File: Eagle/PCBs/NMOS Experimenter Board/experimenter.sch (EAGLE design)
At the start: 0 parts

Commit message: Update packages
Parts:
- added D10, D11, D12, D13, D14, D15, D16, D17, D18, D19, D2, D20, D21, D22, D23, D24, D25, D3, D4, D5, D6, D7, D8, D9: (no value), ellajameson-core:LED0603
- added DRAINA10, DRAINA11, DRAINA12, DRAINA13, DRAINA14, DRAINA15, DRAINA16, DRAINA17, DRAINA18, DRAINA19, DRAINA2, DRAINA20, DRAINA21, DRAINA22, DRAINA23, DRAINA24, DRAINA25, DRAINA3, DRAINA4, DRAINA5, DRAINA6, DRAINA7, DRAINA8, DRAINA9, DRAINB10, DRAINB11, DRAINB12, DRAINB13, DRAINB14, DRAINB15, DRAINB16, DRAINB17, DRAINB18, DRAINB19, DRAINB2, DRAINB20, DRAINB21, DRAINB22, DRAINB23, DRAINB24, DRAINB25, DRAINB3, DRAINB4, DRAINB5, DRAINB6, DRAINB7, DRAINB8, DRAINB9, DRAINC10, DRAINC11, DRAINC12, DRAINC13, DRAINC14, DRAINC15, DRAINC16, DRAINC17, DRAINC18, DRAINC19, DRAINC2, DRAINC20, DRAINC21, DRAINC22, DRAINC23, DRAINC24, DRAINC25, DRAINC3, DRAINC4, DRAINC5, DRAINC6, DRAINC7, DRAINC8, DRAINC9, DRAIND10, DRAIND11, DRAIND12, DRAIND13, DRAIND14, DRAIND15, DRAIND16, DRAIND17, DRAIND18, DRAIND19, DRAIND2, DRAIND20, DRAIND21, DRAIND22, DRAIND23, DRAIND24, DRAIND25, DRAIND3, DRAIND4, DRAIND5, DRAIND6, DRAIND7, DRAIND8, DRAIND9, GATE10, GATE11, GATE12, GATE13, GATE14, GATE15, GATE16, GATE17, GATE18, GATE19, GATE2, GATE20, GATE21, GATE22, GATE23, GATE24, GATE25, GATE3, GATE4, GATE5, GATE6, GATE7, GATE8, GATE9, SOURCEA10, SOURCEA11, SOURCEA12, SOURCEA13, SOURCEA14, SOURCEA15, SOURCEA16, SOURCEA17, SOURCEA18, SOURCEA19, SOURCEA2, SOURCEA20, SOURCEA21, SOURCEA22, SOURCEA23, SOURCEA24, SOURCEA25, SOURCEA3, SOURCEA4, SOURCEA5, SOURCEA6, SOURCEA7, SOURCEA8, SOURCEA9, SOURCEB10, SOURCEB11, SOURCEB12, SOURCEB13, SOURCEB14, SOURCEB15, SOURCEB16, SOURCEB17, SOURCEB18, SOURCEB19, SOURCEB2, SOURCEB20, SOURCEB21, SOURCEB22, SOURCEB23, SOURCEB24, SOURCEB25, SOURCEB3, SOURCEB4, SOURCEB5, SOURCEB6, SOURCEB7, SOURCEB8, SOURCEB9, SOURCEC10, SOURCEC11, SOURCEC12, SOURCEC13, SOURCEC14, SOURCEC15, SOURCEC16, SOURCEC17, SOURCEC18, SOURCEC19, SOURCEC2, SOURCEC20, SOURCEC21, SOURCEC22, SOURCEC23, SOURCEC24, SOURCEC25, SOURCEC3, SOURCEC4, SOURCEC5, SOURCEC6, SOURCEC7, SOURCEC8, SOURCEC9, SOURCED10, SOURCED11, SOURCED12, SOURCED13, SOURCED14, SOURCED15, SOURCED16, SOURCED17, SOURCED18, SOURCED19, SOURCED2, SOURCED20, SOURCED21, SOURCED22, SOURCED23, SOURCED24, SOURCED25, SOURCED3, SOURCED4, SOURCED5, SOURCED6, SOURCED7, SOURCED8, SOURCED9: TPWIRE, ellajameson-core:TPWIRE
- added JD10, JD11, JD12, JD13, JD14, JD15, JD16, JD17, JD18, JD19, JD2, JD20, JD21, JD22, JD23, JD24, JD25, JD3, JD4, JD5, JD6, JD7, JD8, JD9, JN10, JN11, JN12, JN13, JN14, JN15, JN16, JN17, JN18, JN19, JN2, JN20, JN21, JN22, JN23, JN24, JN25, JN3, JN4, JN5, JN6, JN7, JN8, JN9, JP10, JP11, JP12, JP13, JP14, JP15, JP16, JP17, JP18, JP19, JP2, JP20, JP21, JP22, JP23, JP24, JP25, JP3, JP4, JP5, JP6, JP7, JP8, JP9, JS10, JS11, JS12, JS13, JS14, JS15, JS16, JS17, JS18, JS19, JS2, JS20, JS21, JS22, JS23, JS24, JS25, JS3, JS4, JS5, JS6, JS7, JS8, JS9: SJ_NO, ellajameson-core:SJ_NO
- added Q10, Q11, Q12, Q13, Q14, Q15, Q16, Q17, Q18, Q19, Q2, Q20, Q21, Q22, Q23, Q24, Q25, Q3, Q4, Q5, Q6, Q7, Q8, Q9: 2N7002, ellajameson-core:2N7002
- added R10, R11, R12, R13, R14, R15, R16, R17, R18, R19, R2, R20, R21, R22, R23, R24, R25, R3, R4, R5, R6, R7, R8, R9: (no value), ellajameson-core:RES0603
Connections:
- new net GND: JN10.1, JN11.1, JN12.1, JN13.1, JN14.1, JN15.1, JN16.1, JN17.1, JN18.1, JN19.1, JN2.1, JN20.1, JN21.1, JN22.1, JN23.1, JN24.1, JN25.1, JN3.1, JN4.1, JN5.1, JN6.1, JN7.1, JN8.1, JN9.1
- new net N$1: D2.A, JP2.2, R2.1
- new net N$10: D3.K, DRAINA3.S, DRAINB3.S, DRAINC3.S, DRAIND3.S, JD3.2, JD4.1, JP3.1, JS12.1, Q3.D
- new net N$100: GATE25.S, Q25.G
- new net N$11: JN3.2, JS3.2, Q3.S, SOURCEA3.S, SOURCEB3.S, SOURCEC3.S, SOURCED3.S
- new net N$12: GATE3.S, Q3.G
- new net N$13: D4.A, JP4.2, R4.1
- new net N$14: D4.K, DRAINA4.S, DRAINB4.S, DRAINC4.S, DRAIND4.S, JD2.1, JD4.2, JP4.1, JS11.1, Q4.D
- new net N$15: JN4.2, JS4.2, Q4.S, SOURCEA4.S, SOURCEB4.S, SOURCEC4.S, SOURCED4.S
- new net N$16: GATE4.S, Q4.G
- new net N$17: D5.A, JP5.2, R5.1
- new net N$18: D5.K, DRAINA5.S, DRAINB5.S, DRAINC5.S, DRAIND5.S, JD3.1, JD5.2, JP5.1, JS13.1, Q5.D
- new net N$19: JN5.2, JS5.2, Q5.S, SOURCEA5.S, SOURCEB5.S, SOURCEC5.S, SOURCED5.S
- new net N$2: D2.K, DRAINA2.S, DRAINB2.S, DRAINC2.S, DRAIND2.S, JD2.2, JP2.1, JS10.1, Q2.D
- new net N$20: GATE5.S, Q5.G
- new net N$21: D6.A, JP6.2, R6.1
- new net N$22: D6.K, DRAINA6.S, DRAINB6.S, DRAINC6.S, DRAIND6.S, JD5.1, JD6.2, JP6.1, JS14.1, Q6.D
- new net N$23: JN6.2, JS6.2, Q6.S, SOURCEA6.S, SOURCEB6.S, SOURCEC6.S, SOURCED6.S
- new net N$24: GATE6.S, Q6.G
- new net N$25: D7.A, JP7.2, R7.1
- new net N$26: D7.K, DRAINA7.S, DRAINB7.S, DRAINC7.S, DRAIND7.S, JD6.1, JD7.2, JP7.1, JS15.1, Q7.D
- new net N$27: JN7.2, JS7.2, Q7.S, SOURCEA7.S, SOURCEB7.S, SOURCEC7.S, SOURCED7.S
- new net N$28: GATE7.S, Q7.G
- new net N$29: D8.A, JP8.2, R8.1
- new net N$3: JN2.2, JS2.2, Q2.S, SOURCEA2.S, SOURCEB2.S, SOURCEC2.S, SOURCED2.S
- new net N$30: D8.K, DRAINA8.S, DRAINB8.S, DRAINC8.S, DRAIND8.S, JD7.1, JD8.2, JP8.1, JS16.1, Q8.D
- new net N$31: JN8.2, JS8.2, Q8.S, SOURCEA8.S, SOURCEB8.S, SOURCEC8.S, SOURCED8.S
- new net N$32: GATE8.S, Q8.G
- new net N$33: D9.A, JP9.2, R9.1
- new net N$34: D9.K, DRAINA9.S, DRAINB9.S, DRAINC9.S, DRAIND9.S, JD8.1, JD9.2, JP9.1, JS17.1, Q9.D
- new net N$35: JN9.2, JS9.2, Q9.S, SOURCEA9.S, SOURCEB9.S, SOURCEC9.S, SOURCED9.S
- new net N$36: GATE9.S, Q9.G
- new net N$37: D10.A, JP10.2, R10.1
- new net N$38: D10.K, DRAINA10.S, DRAINB10.S, DRAINC10.S, DRAIND10.S, JD10.2, JP10.1, JS18.1, Q10.D
- new net N$39: JN10.2, JS10.2, Q10.S, SOURCEA10.S, SOURCEB10.S, SOURCEC10.S, SOURCED10.S
- new net N$4: GATE2.S, Q2.G
- new net N$40: GATE10.S, Q10.G
- new net N$41: D11.A, JP11.2, R11.1
- new net N$42: D11.K, DRAINA11.S, DRAINB11.S, DRAINC11.S, DRAIND11.S, JD10.1, JD11.2, JP11.1, JS19.1, Q11.D
- new net N$43: JN11.2, JS11.2, Q11.S, SOURCEA11.S, SOURCEB11.S, SOURCEC11.S, SOURCED11.S
- new net N$44: GATE11.S, Q11.G
- new net N$45: D12.A, JP12.2, R12.1
- new net N$46: D12.K, DRAINA12.S, DRAINB12.S, DRAINC12.S, DRAIND12.S, JD11.1, JD12.2, JP12.1, JS20.1, Q12.D
- new net N$47: JN12.2, JS12.2, Q12.S, SOURCEA12.S, SOURCEB12.S, SOURCEC12.S, SOURCED12.S
- new net N$48: GATE12.S, Q12.G
- new net N$49: D13.A, JP13.2, R13.1
- new net N$50: D13.K, DRAINA13.S, DRAINB13.S, DRAINC13.S, DRAIND13.S, JD12.1, JD13.2, JP13.1, JS21.1, Q13.D
- new net N$51: JN13.2, JS13.2, Q13.S, SOURCEA13.S, SOURCEB13.S, SOURCEC13.S, SOURCED13.S
- new net N$52: GATE13.S, Q13.G
- new net N$53: D14.A, JP14.2, R14.1
- new net N$54: D14.K, DRAINA14.S, DRAINB14.S, DRAINC14.S, DRAIND14.S, JD13.1, JD14.2, JP14.1, JS22.1, Q14.D
- new net N$55: JN14.2, JS14.2, Q14.S, SOURCEA14.S, SOURCEB14.S, SOURCEC14.S, SOURCED14.S
- new net N$56: GATE14.S, Q14.G
- new net N$57: D15.A, JP15.2, R15.1
- new net N$58: D15.K, DRAINA15.S, DRAINB15.S, DRAINC15.S, DRAIND15.S, JD14.1, JD15.2, JP15.1, JS23.1, Q15.D
- new net N$59: JN15.2, JS15.2, Q15.S, SOURCEA15.S, SOURCEB15.S, SOURCEC15.S, SOURCED15.S
- new net N$60: GATE15.S, Q15.G
- new net N$61: D16.A, JP16.2, R16.1
- new net N$62: D16.K, DRAINA16.S, DRAINB16.S, DRAINC16.S, DRAIND16.S, JD15.1, JD16.2, JP16.1, JS24.1, Q16.D
- new net N$63: JN16.2, JS16.2, Q16.S, SOURCEA16.S, SOURCEB16.S, SOURCEC16.S, SOURCED16.S
- new net N$64: GATE16.S, Q16.G
- new net N$65: D17.A, JP17.2, R17.1
- new net N$66: D17.K, DRAINA17.S, DRAINB17.S, DRAINC17.S, DRAIND17.S, JD16.1, JD17.2, JP17.1, JS25.1, Q17.D
- new net N$67: JN17.2, JS17.2, Q17.S, SOURCEA17.S, SOURCEB17.S, SOURCEC17.S, SOURCED17.S
- new net N$68: GATE17.S, Q17.G
- new net N$69: D18.A, JP18.2, R18.1
- new net N$70: D18.K, DRAINA18.S, DRAINB18.S, DRAINC18.S, DRAIND18.S, JD18.2, JP18.1, Q18.D
- new net N$71: JN18.2, JS18.2, Q18.S, SOURCEA18.S, SOURCEB18.S, SOURCEC18.S, SOURCED18.S
- new net N$72: GATE18.S, Q18.G
- new net N$73: D19.A, JP19.2, R19.1
- new net N$74: D19.K, DRAINA19.S, DRAINB19.S, DRAINC19.S, DRAIND19.S, JD18.1, JD19.2, JP19.1, Q19.D
- new net N$75: JN19.2, JS19.2, Q19.S, SOURCEA19.S, SOURCEB19.S, SOURCEC19.S, SOURCED19.S
- new net N$76: GATE19.S, Q19.G
- new net N$77: D20.A, JP20.2, R20.1
- new net N$78: D20.K, DRAINA20.S, DRAINB20.S, DRAINC20.S, DRAIND20.S, JD19.1, JD20.2, JP20.1, Q20.D
- new net N$79: JN20.2, JS20.2, Q20.S, SOURCEA20.S, SOURCEB20.S, SOURCEC20.S, SOURCED20.S
- new net N$80: GATE20.S, Q20.G
- new net N$81: D21.A, JP21.2, R21.1
- new net N$82: D21.K, DRAINA21.S, DRAINB21.S, DRAINC21.S, DRAIND21.S, JD20.1, JD21.2, JP21.1, Q21.D
- new net N$83: JN21.2, JS21.2, Q21.S, SOURCEA21.S, SOURCEB21.S, SOURCEC21.S, SOURCED21.S
- new net N$84: GATE21.S, Q21.G
- new net N$85: D22.A, JP22.2, R22.1
- new net N$86: D22.K, DRAINA22.S, DRAINB22.S, DRAINC22.S, DRAIND22.S, JD21.1, JD22.2, JP22.1, Q22.D
- new net N$87: JN22.2, JS22.2, Q22.S, SOURCEA22.S, SOURCEB22.S, SOURCEC22.S, SOURCED22.S
- new net N$88: GATE22.S, Q22.G
- new net N$89: D23.A, JP23.2, R23.1
- new net N$9: D3.A, JP3.2, R3.1
- new net N$90: D23.K, DRAINA23.S, DRAINB23.S, DRAINC23.S, DRAIND23.S, JD22.1, JD23.2, JP23.1, Q23.D
- new net N$91: JN23.2, JS23.2, Q23.S, SOURCEA23.S, SOURCEB23.S, SOURCEC23.S, SOURCED23.S
- new net N$92: GATE23.S, Q23.G
- new net N$93: D24.A, JP24.2, R24.1
- new net N$94: D24.K, DRAINA24.S, DRAINB24.S, DRAINC24.S, DRAIND24.S, JD23.1, JD24.2, JP24.1, Q24.D
- new net N$95: JN24.2, JS24.2, Q24.S, SOURCEA24.S, SOURCEB24.S, SOURCEC24.S, SOURCED24.S
- new net N$96: GATE24.S, Q24.G
- new net N$97: D25.A, JP25.2, R25.1
- new net N$98: D25.K, DRAINA25.S, DRAINB25.S, DRAINC25.S, DRAIND25.S, JD24.1, JD25.2, JP25.1, Q25.D
- new net N$99: JN25.2, JS25.2, Q25.S, SOURCEA25.S, SOURCEB25.S, SOURCEC25.S, SOURCED25.S
- new net VCC: R10.2, R11.2, R12.2, R13.2, R14.2, R15.2, R16.2, R17.2, R18.2, R19.2, R2.2, R20.2, R21.2, R22.2, R23.2, R24.2, R25.2, R3.2, R4.2, R5.2, R6.2, R7.2, R8.2, R9.2
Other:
- note added: "NMOS Logic Transistor Cell"

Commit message: A 6x12 grid fits
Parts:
- added D26, D27, D28, D29, D30, D31, D32, D33, D34, D35, D36, D37, D38, D39, D40, D41, D42, D43, D44, D45, D46, D47, D48, D49, D50, D51, D52, D53, D54, D55, D56, D57, D58, D59, D60, D61, D62, D63, D64, D65, D66, D67, D68, D69, D70, D71, D72, D73: (no value), ellajameson-core:LED0603
- added DRAINA26, DRAINA27, DRAINA28, DRAINA29, DRAINA30, DRAINA31, DRAINA32, DRAINA33, DRAINA34, DRAINA35, DRAINA36, DRAINA37, DRAINA38, DRAINA39, DRAINA40, DRAINA41, DRAINA42, DRAINA43, DRAINA44, DRAINA45, DRAINA46, DRAINA47, DRAINA48, DRAINA49, DRAINA50, DRAINA51, DRAINA52, DRAINA53, DRAINA54, DRAINA55, DRAINA56, DRAINA57, DRAINA58, DRAINA59, DRAINA60, DRAINA61, DRAINA62, DRAINA63, DRAINA64, DRAINA65, DRAINA66, DRAINA67, DRAINA68, DRAINA69, DRAINA70, DRAINA71, DRAINA72, DRAINA73, DRAINB26, DRAINB27, DRAINB28, DRAINB29, DRAINB30, DRAINB31, DRAINB32, DRAINB33, DRAINB34, DRAINB35, DRAINB36, DRAINB37, DRAINB38, DRAINB39, DRAINB40, DRAINB41, DRAINB42, DRAINB43, DRAINB44, DRAINB45, DRAINB46, DRAINB47, DRAINB48, DRAINB49, DRAINB50, DRAINB51, DRAINB52, DRAINB53, DRAINB54, DRAINB55, DRAINB56, DRAINB57, DRAINB58, DRAINB59, DRAINB60, DRAINB61, DRAINB62, DRAINB63, DRAINB64, DRAINB65, DRAINB66, DRAINB67, DRAINB68, DRAINB69, DRAINB70, DRAINB71, DRAINB72, DRAINB73, DRAINC26, DRAINC27, DRAINC28, DRAINC29, DRAINC30, DRAINC31, DRAINC32, DRAINC33, DRAINC34, DRAINC35, DRAINC36, DRAINC37, DRAINC38, DRAINC39, DRAINC40, DRAINC41, DRAINC42, DRAINC43, DRAINC44, DRAINC45, DRAINC46, DRAINC47, DRAINC48, DRAINC49, DRAINC50, DRAINC51, DRAINC52, DRAINC53, DRAINC54, DRAINC55, DRAINC56, DRAINC57, DRAINC58, DRAINC59, DRAINC60, DRAINC61, DRAINC62, DRAINC63, DRAINC64, DRAINC65, DRAINC66, DRAINC67, DRAINC68, DRAINC69, DRAINC70, DRAINC71, DRAINC72, DRAINC73, DRAIND26, DRAIND27, DRAIND28, DRAIND29, DRAIND30, DRAIND31, DRAIND32, DRAIND33, DRAIND34, DRAIND35, DRAIND36, DRAIND37, DRAIND38, DRAIND39, DRAIND40, DRAIND41, DRAIND42, DRAIND43, DRAIND44, DRAIND45, DRAIND46, DRAIND47, DRAIND48, DRAIND49, DRAIND50, DRAIND51, DRAIND52, DRAIND53, DRAIND54, DRAIND55, DRAIND56, DRAIND57, DRAIND58, DRAIND59, DRAIND60, DRAIND61, DRAIND62, DRAIND63, DRAIND64, DRAIND65, DRAIND66, DRAIND67, DRAIND68, DRAIND69, DRAIND70, DRAIND71, DRAIND72, DRAIND73, GATE26, GATE27, GATE28, GATE29, GATE30, GATE31, GATE32, GATE33, GATE34, GATE35, GATE36, GATE37, GATE38, GATE39, GATE40, GATE41, GATE42, GATE43, GATE44, GATE45, GATE46, GATE47, GATE48, GATE49, GATE50, GATE51, GATE52, GATE53, GATE54, GATE55, GATE56, GATE57, GATE58, GATE59, GATE60, GATE61, GATE62, GATE63, GATE64, GATE65, GATE66, GATE67, GATE68, GATE69, GATE70, GATE71, GATE72, GATE73, SOURCEA26, SOURCEA27, SOURCEA28, SOURCEA29, SOURCEA30, SOURCEA31, SOURCEA32, SOURCEA33, SOURCEA34, SOURCEA35, SOURCEA36, SOURCEA37, SOURCEA38, SOURCEA39, SOURCEA40, SOURCEA41, SOURCEA42, SOURCEA43, SOURCEA44, SOURCEA45, SOURCEA46, SOURCEA47, SOURCEA48, SOURCEA49, SOURCEA50, SOURCEA51, SOURCEA52, SOURCEA53, SOURCEA54, SOURCEA55, SOURCEA56, SOURCEA57, SOURCEA58, SOURCEA59, SOURCEA60, SOURCEA61, SOURCEA62, SOURCEA63, SOURCEA64, SOURCEA65, SOURCEA66, SOURCEA67, SOURCEA68, SOURCEA69, SOURCEA70, SOURCEA71, SOURCEA72, SOURCEA73, SOURCEB26, SOURCEB27, SOURCEB28, SOURCEB29, SOURCEB30, SOURCEB31, SOURCEB32, SOURCEB33, SOURCEB34, SOURCEB35, SOURCEB36, SOURCEB37, SOURCEB38, SOURCEB39, SOURCEB40, SOURCEB41, SOURCEB42, SOURCEB43, SOURCEB44, SOURCEB45, SOURCEB46, SOURCEB47, SOURCEB48, SOURCEB49, SOURCEB50, SOURCEB51, SOURCEB52, SOURCEB53, SOURCEB54, SOURCEB55, SOURCEB56, SOURCEB57, SOURCEB58, SOURCEB59, SOURCEB60, SOURCEB61, SOURCEB62, SOURCEB63, SOURCEB64, SOURCEB65, SOURCEB66, SOURCEB67, SOURCEB68, SOURCEB69, SOURCEB70, SOURCEB71, SOURCEB72, SOURCEB73, SOURCEC26, SOURCEC27, SOURCEC28, SOURCEC29, SOURCEC30, SOURCEC31, SOURCEC32, SOURCEC33, SOURCEC34, SOURCEC35, SOURCEC36, SOURCEC37, SOURCEC38, SOURCEC39, SOURCEC40, SOURCEC41, SOURCEC42, SOURCEC43, SOURCEC44, SOURCEC45, SOURCEC46, SOURCEC47, SOURCEC48, SOURCEC49, SOURCEC50, SOURCEC51, SOURCEC52, SOURCEC53, SOURCEC54, SOURCEC55, SOURCEC56, SOURCEC57, SOURCEC58, SOURCEC59, SOURCEC60, SOURCEC61, SOURCEC62, SOURCEC63, SOURCEC64, SOURCEC65, SOURCEC66, SOURCEC67, SOURCEC68, SOURCEC69, SOURCEC70, SOURCEC71, SOURCEC72, SOURCEC73, SOURCED26, SOURCED27, SOURCED28, SOURCED29, SOURCED30, SOURCED31, SOURCED32, SOURCED33, SOURCED34, SOURCED35, SOURCED36, SOURCED37, SOURCED38, SOURCED39, SOURCED40, SOURCED41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: TPWIRE, ellajameson-core:TPWIRE
- added JD26, JD27, JD28, JD29, JD30, JD31, JD32, JD33, JD34, JD35, JD36, JD37, JD38, JD39, JD40, JD41, JD42, JD43, JD44, JD45, JD46, JD47, JD48, JD49, JD50, JD51, JD52, JD53, JD54, JD55, JD56, JD57, JD58, JD59, JD60, JD61, JD62, JD63, JD64, JD65, JD66, JD67, JD68, JD69, JD70, JD71, JD72, JD73, JN26, JN27, JN28, JN29, JN30, JN31, JN32, JN33, JN34, JN35, JN36, JN37, JN38, JN39, JN40, JN41, JN42, JN43, JN44, JN45, JN46, JN47, JN48, JN49, JN50, JN51, JN52, JN53, JN54, JN55, JN56, JN57, JN58, JN59, JN60, JN61, JN62, JN63, JN64, JN65, JN66, JN67, JN68, JN69, JN70, JN71, JN72, JN73, JP26, JP27, JP28, JP29, JP30, JP31, JP32, JP33, JP34, JP35, JP36, JP37, JP38, JP39, JP40, JP41, JP42, JP43, JP44, JP45, JP46, JP47, JP48, JP49, JP50, JP51, JP52, JP53, JP54, JP55, JP56, JP57, JP58, JP59, JP60, JP61, JP62, JP63, JP64, JP65, JP66, JP67, JP68, JP69, JP70, JP71, JP72, JP73, JS26, JS27, JS28, JS29, JS30, JS31, JS32, JS33, JS34, JS35, JS36, JS37, JS38, JS39, JS40, JS41, JS42, JS43, JS44, JS45, JS46, JS47, JS48, JS49, JS50, JS51, JS52, JS53, JS54, JS55, JS56, JS57, JS58, JS59, JS60, JS61, JS62, JS63, JS64, JS65, JS66, JS67, JS68, JS69, JS70, JS71, JS72, JS73: SJ_NO, ellajameson-core:SJ_NO
- added Q26, Q27, Q28, Q29, Q30, Q31, Q32, Q33, Q34, Q35, Q36, Q37, Q38, Q39, Q40, Q41, Q42, Q43, Q44, Q45, Q46, Q47, Q48, Q49, Q50, Q51, Q52, Q53, Q54, Q55, Q56, Q57, Q58, Q59, Q60, Q61, Q62, Q63, Q64, Q65, Q66, Q67, Q68, Q69, Q70, Q71, Q72, Q73: 2N7002, ellajameson-core:2N7002
- added R26, R27, R28, R29, R30, R31, R32, R33, R34, R35, R36, R37, R38, R39, R40, R41, R42, R43, R44, R45, R46, R47, R48, R49, R50, R51, R52, R53, R54, R55, R56, R57, R58, R59, R60, R61, R62, R63, R64, R65, R66, R67, R68, R69, R70, R71, R72, R73: (no value), ellajameson-core:RES0603
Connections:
- new net N$101: D26.A, JP26.2, R26.1
- new net N$102: D26.K, DRAINA26.S, DRAINB26.S, DRAINC26.S, DRAIND26.S, JD26.2, JP26.1, JS34.1, Q26.D
- new net N$103: JN26.2, JS26.2, Q26.S, SOURCEA26.S, SOURCEB26.S, SOURCEC26.S, SOURCED26.S
- new net N$104: GATE26.S, Q26.G
- new net N$105: D27.A, JP27.2, R27.1
- new net N$106: D27.K, DRAINA27.S, DRAINB27.S, DRAINC27.S, DRAIND27.S, JD26.1, JD27.2, JP27.1, JS35.1, Q27.D
- new net N$107: JN27.2, JS27.2, Q27.S, SOURCEA27.S, SOURCEB27.S, SOURCEC27.S, SOURCED27.S
- new net N$108: GATE27.S, Q27.G
- new net N$109: D28.A, JP28.2, R28.1
- new net N$110: D28.K, DRAINA28.S, DRAINB28.S, DRAINC28.S, DRAIND28.S, JD27.1, JD28.2, JP28.1, JS36.1, Q28.D
- new net N$111: JN28.2, JS28.2, Q28.S, SOURCEA28.S, SOURCEB28.S, SOURCEC28.S, SOURCED28.S
- new net N$112: GATE28.S, Q28.G
- new net N$113: D29.A, JP29.2, R29.1
- new net N$114: D29.K, DRAINA29.S, DRAINB29.S, DRAINC29.S, DRAIND29.S, JD28.1, JD29.2, JP29.1, JS37.1, Q29.D
- new net N$115: JN29.2, JS29.2, Q29.S, SOURCEA29.S, SOURCEB29.S, SOURCEC29.S, SOURCED29.S
- new net N$116: GATE29.S, Q29.G
- new net N$117: D30.A, JP30.2, R30.1
- new net N$118: D30.K, DRAINA30.S, DRAINB30.S, DRAINC30.S, DRAIND30.S, JD29.1, JD30.2, JP30.1, JS38.1, Q30.D
- new net N$119: JN30.2, JS30.2, Q30.S, SOURCEA30.S, SOURCEB30.S, SOURCEC30.S, SOURCED30.S
- new net N$120: GATE30.S, Q30.G
- new net N$121: D31.A, JP31.2, R31.1
- new net N$122: D31.K, DRAINA31.S, DRAINB31.S, DRAINC31.S, DRAIND31.S, JD30.1, JD31.2, JP31.1, JS39.1, Q31.D
- new net N$123: JN31.2, JS31.2, Q31.S, SOURCEA31.S, SOURCEB31.S, SOURCEC31.S, SOURCED31.S
- new net N$124: GATE31.S, Q31.G
- new net N$125: D32.A, JP32.2, R32.1
- new net N$126: D32.K, DRAINA32.S, DRAINB32.S, DRAINC32.S, DRAIND32.S, JD31.1, JD32.2, JP32.1, JS40.1, Q32.D
- new net N$127: JN32.2, JS32.2, Q32.S, SOURCEA32.S, SOURCEB32.S, SOURCEC32.S, SOURCED32.S
- new net N$128: GATE32.S, Q32.G
- new net N$129: D33.A, JP33.2, R33.1
- new net N$130: D33.K, DRAINA33.S, DRAINB33.S, DRAINC33.S, DRAIND33.S, JD32.1, JD33.2, JP33.1, JS41.1, Q33.D
- new net N$131: JN33.2, JS33.2, Q33.S, SOURCEA33.S, SOURCEB33.S, SOURCEC33.S, SOURCED33.S
- new net N$132: GATE33.S, Q33.G
- new net N$133: D34.A, JP34.2, R34.1
- new net N$134: D34.K, DRAINA34.S, DRAINB34.S, DRAINC34.S, DRAIND34.S, JD34.2, JP34.1, JS42.1, Q34.D
- new net N$135: JN34.2, JS34.2, Q34.S, SOURCEA34.S, SOURCEB34.S, SOURCEC34.S, SOURCED34.S
- new net N$136: GATE34.S, Q34.G
- new net N$137: D35.A, JP35.2, R35.1
- new net N$138: D35.K, DRAINA35.S, DRAINB35.S, DRAINC35.S, DRAIND35.S, JD34.1, JD35.2, JP35.1, JS43.1, Q35.D
- new net N$139: JN35.2, JS35.2, Q35.S, SOURCEA35.S, SOURCEB35.S, SOURCEC35.S, SOURCED35.S
- new net N$140: GATE35.S, Q35.G
- new net N$141: D36.A, JP36.2, R36.1
- new net N$142: D36.K, DRAINA36.S, DRAINB36.S, DRAINC36.S, DRAIND36.S, JD35.1, JD36.2, JP36.1, JS44.1, Q36.D
- new net N$143: JN36.2, JS36.2, Q36.S, SOURCEA36.S, SOURCEB36.S, SOURCEC36.S, SOURCED36.S
- new net N$144: GATE36.S, Q36.G
- new net N$145: D37.A, JP37.2, R37.1
- new net N$146: D37.K, DRAINA37.S, DRAINB37.S, DRAINC37.S, DRAIND37.S, JD36.1, JD37.2, JP37.1, JS45.1, Q37.D
- new net N$147: JN37.2, JS37.2, Q37.S, SOURCEA37.S, SOURCEB37.S, SOURCEC37.S, SOURCED37.S
- new net N$148: GATE37.S, Q37.G
- new net N$149: D38.A, JP38.2, R38.1
- new net N$150: D38.K, DRAINA38.S, DRAINB38.S, DRAINC38.S, DRAIND38.S, JD37.1, JD38.2, JP38.1, JS46.1, Q38.D
- new net N$151: JN38.2, JS38.2, Q38.S, SOURCEA38.S, SOURCEB38.S, SOURCEC38.S, SOURCED38.S
- new net N$152: GATE38.S, Q38.G
- new net N$153: D39.A, JP39.2, R39.1
- new net N$154: D39.K, DRAINA39.S, DRAINB39.S, DRAINC39.S, DRAIND39.S, JD38.1, JD39.2, JP39.1, JS47.1, Q39.D
- new net N$155: JN39.2, JS39.2, Q39.S, SOURCEA39.S, SOURCEB39.S, SOURCEC39.S, SOURCED39.S
- new net N$156: GATE39.S, Q39.G
- new net N$157: D40.A, JP40.2, R40.1
- new net N$158: D40.K, DRAINA40.S, DRAINB40.S, DRAINC40.S, DRAIND40.S, JD39.1, JD40.2, JP40.1, JS48.1, Q40.D
- new net N$159: JN40.2, JS40.2, Q40.S, SOURCEA40.S, SOURCEB40.S, SOURCEC40.S, SOURCED40.S
- new net N$160: GATE40.S, Q40.G
- new net N$161: D41.A, JP41.2, R41.1
- new net N$162: D41.K, DRAINA41.S, DRAINB41.S, DRAINC41.S, DRAIND41.S, JD40.1, JD41.2, JP41.1, JS49.1, Q41.D
- new net N$163: JN41.2, JS41.2, Q41.S, SOURCEA41.S, SOURCEB41.S, SOURCEC41.S, SOURCED41.S
- new net N$164: GATE41.S, Q41.G
- new net N$165: D42.A, JP42.2, R42.1
- new net N$166: D42.K, DRAINA42.S, DRAINB42.S, DRAINC42.S, DRAIND42.S, JD42.2, JP42.1, JS50.1, Q42.D
- new net N$167: JN42.2, JS42.2, Q42.S, SOURCEA42.S, SOURCEB42.S, SOURCEC42.S, SOURCED42.S
- new net N$168: GATE42.S, Q42.G
- new net N$169: D43.A, JP43.2, R43.1
- new net N$170: D43.K, DRAINA43.S, DRAINB43.S, DRAINC43.S, DRAIND43.S, JD42.1, JD43.2, JP43.1, JS51.1, Q43.D
- new net N$171: JN43.2, JS43.2, Q43.S, SOURCEA43.S, SOURCEB43.S, SOURCEC43.S, SOURCED43.S
- new net N$172: GATE43.S, Q43.G
- new net N$173: D44.A, JP44.2, R44.1
- new net N$174: D44.K, DRAINA44.S, DRAINB44.S, DRAINC44.S, DRAIND44.S, JD43.1, JD44.2, JP44.1, JS52.1, Q44.D
- new net N$175: JN44.2, JS44.2, Q44.S, SOURCEA44.S, SOURCEB44.S, SOURCEC44.S, SOURCED44.S
- new net N$176: GATE44.S, Q44.G
- new net N$177: D45.A, JP45.2, R45.1
- new net N$178: D45.K, DRAINA45.S, DRAINB45.S, DRAINC45.S, DRAIND45.S, JD44.1, JD45.2, JP45.1, JS53.1, Q45.D
- new net N$179: JN45.2, JS45.2, Q45.S, SOURCEA45.S, SOURCEB45.S, SOURCEC45.S, SOURCED45.S
- new net N$180: GATE45.S, Q45.G
- new net N$181: D46.A, JP46.2, R46.1
- new net N$182: D46.K, DRAINA46.S, DRAINB46.S, DRAINC46.S, DRAIND46.S, JD45.1, JD46.2, JP46.1, JS54.1, Q46.D
- new net N$183: JN46.2, JS46.2, Q46.S, SOURCEA46.S, SOURCEB46.S, SOURCEC46.S, SOURCED46.S
- new net N$184: GATE46.S, Q46.G
- new net N$185: D47.A, JP47.2, R47.1
- new net N$186: D47.K, DRAINA47.S, DRAINB47.S, DRAINC47.S, DRAIND47.S, JD46.1, JD47.2, JP47.1, JS55.1, Q47.D
- new net N$187: JN47.2, JS47.2, Q47.S, SOURCEA47.S, SOURCEB47.S, SOURCEC47.S, SOURCED47.S
- new net N$188: GATE47.S, Q47.G
- new net N$189: D48.A, JP48.2, R48.1
- new net N$190: D48.K, DRAINA48.S, DRAINB48.S, DRAINC48.S, DRAIND48.S, JD47.1, JD48.2, JP48.1, JS56.1, Q48.D
- new net N$191: JN48.2, JS48.2, Q48.S, SOURCEA48.S, SOURCEB48.S, SOURCEC48.S, SOURCED48.S
- new net N$192: GATE48.S, Q48.G
- new net N$193: D49.A, JP49.2, R49.1
- new net N$194: D49.K, DRAINA49.S, DRAINB49.S, DRAINC49.S, DRAIND49.S, JD48.1, JD49.2, JP49.1, JS57.1, Q49.D
- new net N$195: JN49.2, JS49.2, Q49.S, SOURCEA49.S, SOURCEB49.S, SOURCEC49.S, SOURCED49.S
- new net N$196: GATE49.S, Q49.G
- new net N$197: D50.A, JP50.2, R50.1
- new net N$198: D50.K, DRAINA50.S, DRAINB50.S, DRAINC50.S, DRAIND50.S, JD50.2, JP50.1, JS58.1, Q50.D
- new net N$199: JN50.2, JS50.2, Q50.S, SOURCEA50.S, SOURCEB50.S, SOURCEC50.S, SOURCED50.S
- new net N$200: GATE50.S, Q50.G
- new net N$201: D51.A, JP51.2, R51.1
- new net N$202: D51.K, DRAINA51.S, DRAINB51.S, DRAINC51.S, DRAIND51.S, JD50.1, JD51.2, JP51.1, JS59.1, Q51.D
- new net N$203: JN51.2, JS51.2, Q51.S, SOURCEA51.S, SOURCEB51.S, SOURCEC51.S, SOURCED51.S
- new net N$204: GATE51.S, Q51.G
- new net N$205: D52.A, JP52.2, R52.1
- new net N$206: D52.K, DRAINA52.S, DRAINB52.S, DRAINC52.S, DRAIND52.S, JD51.1, JD52.2, JP52.1, JS60.1, Q52.D
- new net N$207: JN52.2, JS52.2, Q52.S, SOURCEA52.S, SOURCEB52.S, SOURCEC52.S, SOURCED52.S
- new net N$208: GATE52.S, Q52.G
- new net N$209: D53.A, JP53.2, R53.1
- new net N$210: D53.K, DRAINA53.S, DRAINB53.S, DRAINC53.S, DRAIND53.S, JD52.1, JD53.2, JP53.1, JS61.1, Q53.D
- new net N$211: JN53.2, JS53.2, Q53.S, SOURCEA53.S, SOURCEB53.S, SOURCEC53.S, SOURCED53.S
- new net N$212: GATE53.S, Q53.G
- new net N$213: D54.A, JP54.2, R54.1
- new net N$214: D54.K, DRAINA54.S, DRAINB54.S, DRAINC54.S, DRAIND54.S, JD53.1, JD54.2, JP54.1, JS62.1, Q54.D
- new net N$215: JN54.2, JS54.2, Q54.S, SOURCEA54.S, SOURCEB54.S, SOURCEC54.S, SOURCED54.S
- new net N$216: GATE54.S, Q54.G
- new net N$217: D55.A, JP55.2, R55.1
- new net N$218: D55.K, DRAINA55.S, DRAINB55.S, DRAINC55.S, DRAIND55.S, JD54.1, JD55.2, JP55.1, JS63.1, Q55.D
- new net N$219: JN55.2, JS55.2, Q55.S, SOURCEA55.S, SOURCEB55.S, SOURCEC55.S, SOURCED55.S
- new net N$220: GATE55.S, Q55.G
- new net N$221: D56.A, JP56.2, R56.1
- new net N$222: D56.K, DRAINA56.S, DRAINB56.S, DRAINC56.S, DRAIND56.S, JD55.1, JD56.2, JP56.1, JS64.1, Q56.D
- new net N$223: JN56.2, JS56.2, Q56.S, SOURCEA56.S, SOURCEB56.S, SOURCEC56.S, SOURCED56.S
- new net N$224: GATE56.S, Q56.G
- new net N$225: D57.A, JP57.2, R57.1
- new net N$226: D57.K, DRAINA57.S, DRAINB57.S, DRAINC57.S, DRAIND57.S, JD56.1, JD57.2, JP57.1, JS65.1, Q57.D
- new net N$227: JN57.2, JS57.2, Q57.S, SOURCEA57.S, SOURCEB57.S, SOURCEC57.S, SOURCED57.S
- new net N$228: GATE57.S, Q57.G
- new net N$229: D58.A, JP58.2, R58.1
- new net N$230: D58.K, DRAINA58.S, DRAINB58.S, DRAINC58.S, DRAIND58.S, JD58.2, JP58.1, Q58.D
- new net N$231: JN58.2, JS58.2, Q58.S, SOURCEA58.S, SOURCEB58.S, SOURCEC58.S, SOURCED58.S
- new net N$232: GATE58.S, Q58.G
- new net N$233: D59.A, JP59.2, R59.1
- new net N$234: D59.K, DRAINA59.S, DRAINB59.S, DRAINC59.S, DRAIND59.S, JD58.1, JD59.2, JP59.1, Q59.D
- new net N$235: JN59.2, JS59.2, Q59.S, SOURCEA59.S, SOURCEB59.S, SOURCEC59.S, SOURCED59.S
- new net N$236: GATE59.S, Q59.G
- new net N$237: D60.A, JP60.2, R60.1
- new net N$238: D60.K, DRAINA60.S, DRAINB60.S, DRAINC60.S, DRAIND60.S, JD59.1, JD60.2, JP60.1, Q60.D
- new net N$239: JN60.2, JS60.2, Q60.S, SOURCEA60.S, SOURCEB60.S, SOURCEC60.S, SOURCED60.S
- new net N$240: GATE60.S, Q60.G
- new net N$241: D61.A, JP61.2, R61.1
- new net N$242: D61.K, DRAINA61.S, DRAINB61.S, DRAINC61.S, DRAIND61.S, JD60.1, JD61.2, JP61.1, Q61.D
- new net N$243: JN61.2, JS61.2, Q61.S, SOURCEA61.S, SOURCEB61.S, SOURCEC61.S, SOURCED61.S
- new net N$244: GATE61.S, Q61.G
- new net N$245: D62.A, JP62.2, R62.1
- new net N$246: D62.K, DRAINA62.S, DRAINB62.S, DRAINC62.S, DRAIND62.S, JD61.1, JD62.2, JP62.1, Q62.D
- new net N$247: JN62.2, JS62.2, Q62.S, SOURCEA62.S, SOURCEB62.S, SOURCEC62.S, SOURCED62.S
- new net N$248: GATE62.S, Q62.G
- new net N$249: D63.A, JP63.2, R63.1
- new net N$250: D63.K, DRAINA63.S, DRAINB63.S, DRAINC63.S, DRAIND63.S, JD62.1, JD63.2, JP63.1, Q63.D
- new net N$251: JN63.2, JS63.2, Q63.S, SOURCEA63.S, SOURCEB63.S, SOURCEC63.S, SOURCED63.S
- new net N$252: GATE63.S, Q63.G
- new net N$253: D64.A, JP64.2, R64.1
- new net N$254: D64.K, DRAINA64.S, DRAINB64.S, DRAINC64.S, DRAIND64.S, JD63.1, JD64.2, JP64.1, Q64.D
- new net N$255: JN64.2, JS64.2, Q64.S, SOURCEA64.S, SOURCEB64.S, SOURCEC64.S, SOURCED64.S
- new net N$256: GATE64.S, Q64.G
- new net N$257: D65.A, JP65.2, R65.1
- new net N$258: D65.K, DRAINA65.S, DRAINB65.S, DRAINC65.S, DRAIND65.S, JD64.1, JD65.2, JP65.1, Q65.D
- new net N$259: JN65.2, JS65.2, Q65.S, SOURCEA65.S, SOURCEB65.S, SOURCEC65.S, SOURCED65.S
- new net N$260: GATE65.S, Q65.G
- new net N$261: D66.A, JP66.2, R66.1
- new net N$262: D66.K, DRAINA66.S, DRAINB66.S, DRAINC66.S, DRAIND66.S, JD66.2, JD7.1, JP66.1, JS68.1, Q66.D
- new net N$263: JN66.2, JS66.2, Q66.S, SOURCEA66.S, SOURCEB66.S, SOURCEC66.S, SOURCED66.S
- new net N$264: GATE66.S, Q66.G
- new net N$265: D67.A, JP67.2, R67.1
- new net N$266: D67.K, DRAINA67.S, DRAINB67.S, DRAINC67.S, DRAIND67.S, JD66.1, JD67.2, JP67.1, JS69.1, Q67.D
- new net N$267: JN67.2, JS67.2, Q67.S, SOURCEA67.S, SOURCEB67.S, SOURCEC67.S, SOURCED67.S
- new net N$268: GATE67.S, Q67.G
- new net N$269: D68.A, JP68.2, R68.1
- new net N$270: D68.K, DRAINA68.S, DRAINB68.S, DRAINC68.S, DRAIND68.S, JD68.2, JD9.1, JP68.1, JS70.1, Q68.D
- new net N$271: JN68.2, JS68.2, Q68.S, SOURCEA68.S, SOURCEB68.S, SOURCEC68.S, SOURCED68.S
- new net N$272: GATE68.S, Q68.G
- new net N$273: D69.A, JP69.2, R69.1
- new net N$274: D69.K, DRAINA69.S, DRAINB69.S, DRAINC69.S, DRAIND69.S, JD68.1, JD69.2, JP69.1, JS71.1, Q69.D
- new net N$275: JN69.2, JS69.2, Q69.S, SOURCEA69.S, SOURCEB69.S, SOURCEC69.S, SOURCED69.S
- new net N$276: GATE69.S, Q69.G
- new net N$277: D70.A, JP70.2, R70.1
- new net N$278: D70.K, DRAINA70.S, DRAINB70.S, DRAINC70.S, DRAIND70.S, JD11.1, JD70.2, JP70.1, JS72.1, Q70.D
- new net N$279: JN70.2, JS70.2, Q70.S, SOURCEA70.S, SOURCEB70.S, SOURCEC70.S, SOURCED70.S
- new net N$280: GATE70.S, Q70.G
- new net N$281: D71.A, JP71.2, R71.1
- new net N$282: D71.K, DRAINA71.S, DRAINB71.S, DRAINC71.S, DRAIND71.S, JD70.1, JD71.2, JP71.1, JS73.1, Q71.D
- new net N$283: JN71.2, JS71.2, Q71.S, SOURCEA71.S, SOURCEB71.S, SOURCEC71.S, SOURCED71.S
- new net N$284: GATE71.S, Q71.G
- new net N$285: D72.A, JP72.2, R72.1
- new net N$286: D72.K, DRAINA72.S, DRAINB72.S, DRAINC72.S, DRAIND72.S, JD13.1, JD72.2, JP72.1, Q72.D
- new net N$287: JN72.2, JS72.2, Q72.S, SOURCEA72.S, SOURCEB72.S, SOURCEC72.S, SOURCED72.S
- new net N$288: GATE72.S, Q72.G
- new net N$289: D73.A, JP73.2, R73.1
- new net N$290: D73.K, DRAINA73.S, DRAINB73.S, DRAINC73.S, DRAIND73.S, JD72.1, JD73.2, JP73.1, Q73.D
- new net N$291: JN73.2, JS73.2, Q73.S, SOURCEA73.S, SOURCEB73.S, SOURCEC73.S, SOURCED73.S
- new net N$292: GATE73.S, Q73.G
- net GND: now also JN26.1, JN27.1, JN28.1, JN29.1, JN30.1, JN31.1, JN32.1, JN33.1, JN34.1, JN35.1, JN36.1, JN37.1, JN38.1, JN39.1, JN40.1, JN41.1, JN42.1, JN43.1, JN44.1, JN45.1, JN46.1, JN47.1, JN48.1, JN49.1, JN50.1, JN51.1, JN52.1, JN53.1, JN54.1, JN55.1, JN56.1, JN57.1, JN58.1, JN59.1, JN60.1, JN61.1, JN62.1, JN63.1, JN64.1, JN65.1, JN66.1, JN67.1, JN68.1, JN69.1, JN70.1, JN71.1, JN72.1, JN73.1
- net N$10: now also JD2.1, JS5.1; no longer JD4.1, JS12.1
- net N$14: now also JD33.1, JS6.1; no longer JD2.1, JS11.1
- net N$18: now also JD4.1, JS7.1; no longer JD3.1, JS13.1
- net N$2: now also JD25.1, JS4.1; no longer JS10.1
- net N$22: now also JD41.1, JS8.1; no longer JD5.1, JS14.1
- net N$26: now also JS9.1; no longer JS15.1
- net N$30: now also JD49.1, JS10.1; no longer JD7.1, JS16.1
- net N$34: now also JS11.1; no longer JS17.1
- net N$38: now also JD57.1, JS12.1; no longer JS18.1
- net N$42: now also JS13.1; no longer JS19.1
- net N$46: now also JD65.1; no longer JD11.1, JS20.1
- net N$50: no longer JS21.1
- net N$54: now also JD3.1, JS17.1; no longer JD13.1, JS22.1
- net N$58: now also JS16.1; no longer JS23.1
- net N$62: now also JD17.1, JS67.1; no longer JD15.1, JS24.1
- net N$66: now also JD5.1, JS66.1; no longer JD16.1, JS25.1
- net N$70: now also JS26.1
- net N$74: now also JS27.1
- net N$78: now also JS28.1
- net N$82: now also JS29.1
- net N$86: now also JS30.1
- net N$90: now also JS31.1
- net N$94: now also JS32.1
- net N$98: now also JS33.1
- net VCC: now also R26.2, R27.2, R28.2, R29.2, R30.2, R31.2, R32.2, R33.2, R34.2, R35.2, R36.2, R37.2, R38.2, R39.2, R40.2, R41.2, R42.2, R43.2, R44.2, R45.2, R46.2, R47.2, R48.2, R49.2, R50.2, R51.2, R52.2, R53.2, R54.2, R55.2, R56.2, R57.2, R58.2, R59.2, R60.2, R61.2, R62.2, R63.2, R64.2, R65.2, R66.2, R67.2, R68.2, R69.2, R70.2, R71.2, R72.2, R73.2
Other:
- moved on the sheet: D10, D11, D12, D13, D14, D15, D16, D17, D2, D3, D4, D5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

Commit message: Removed useless jumpers
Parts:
- removed JD15, JD16, JD67, JD69, JD71, JD73, JS14, JS15, JS18, JS19, JS2, JS20, JS21, JS22, JS23, JS24, JS25, JS3: SJ_NO, ellajameson-core:SJ_NO
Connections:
- net N$11: no longer JS3.2
- net N$266: no longer JD67.2
- net N$274: no longer JD69.2
- net N$282: no longer JD71.2
- net N$290: no longer JD73.2
- net N$3: no longer JS2.2
- net N$55: no longer JS14.2
- net N$58: no longer JD15.2
- net N$59: no longer JS15.2
- net N$62: no longer JD16.2
- net N$71: no longer JS18.2
- net N$75: no longer JS19.2
- net N$79: no longer JS20.2
- net N$83: no longer JS21.2
- net N$87: no longer JS22.2
- net N$91: no longer JS23.2
- net N$95: no longer JS24.2
- net N$99: no longer JS25.2

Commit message: Added 6x buttons with debouncing
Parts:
- added B1, B2, B3, B4, B5, B6: TPWIRE, ellajameson-core:TPWIRE
- added C11, C2, C3, C5, C7, C9: 0.1u, ellajameson-core:CAP0603
- added R75, R76, R77, R78, R81, R82, R85, R86, R89, R90, R93, R94: 10k, ellajameson-core:RES0603
- added S11, S2, S3, S5, S7, S9: (no value), ellajameson-core:SWITCH-NO-MOMPTS815SJM250SMTRLFS
- added U1: 74HC14PW, ellajameson-core:74HC14PW
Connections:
- new net N$293: R77.1, R78.2, S3.S
- new net N$294: C3.1, R78.1, U1E.I
- new net N$295: B4.S, U1C.O
- new net N$296: B3.S, U1D.O
- new net N$297: R81.1, R82.2, S5.S
- new net N$298: C5.1, R82.1, U1D.I
- new net N$299: B2.S, U1E.O
- new net N$300: B1.S, U1F.O
- new net N$301: R85.1, R86.2, S7.S
- new net N$302: C7.1, R86.1, U1C.I
- new net N$305: R89.1, R90.2, S9.S
- new net N$306: C9.1, R90.1, U1B.I
- new net N$309: R93.1, R94.2, S11.S
- new net N$310: C11.1, R94.1, U1A.I
- new net N$5: B6.S, U1A.O
- new net N$6: B5.S, U1B.O
- new net N$7: R75.1, R76.2, S2.S
- new net N$8: C2.1, R76.1, U1F.I
- net GND: now also C11.2, C2.2, C3.2, C5.2, C7.2, C9.2, S11.P, S2.P, S3.P, S5.P, S7.P, S9.P, U1G$1.V-
- net VCC: now also R75.2, R77.2, R81.2, R85.2, R89.2, R93.2, U1G$1.V+
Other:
- note added: "BUTTON (Simple)"

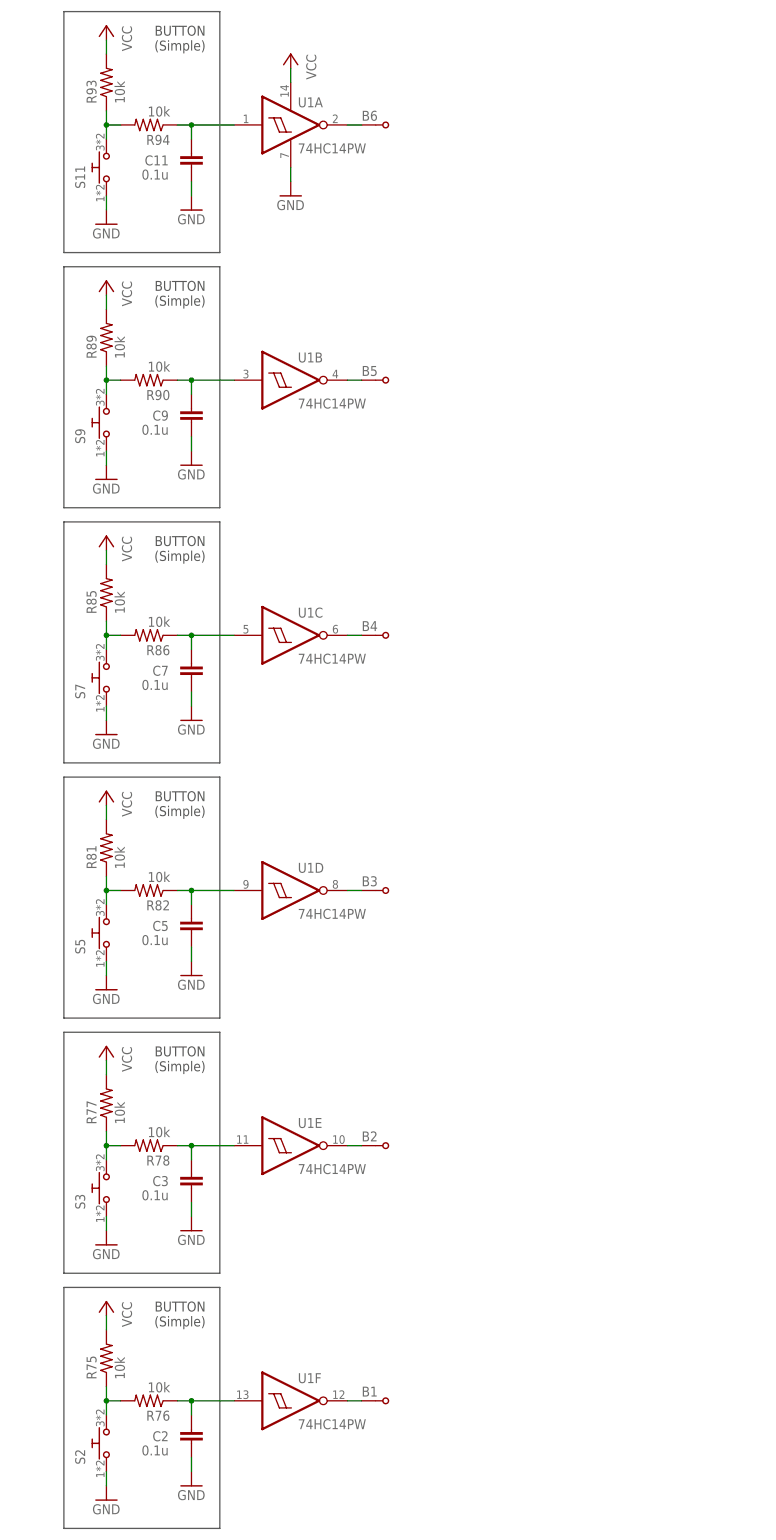
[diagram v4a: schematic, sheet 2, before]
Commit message: Added basic power and stripboard
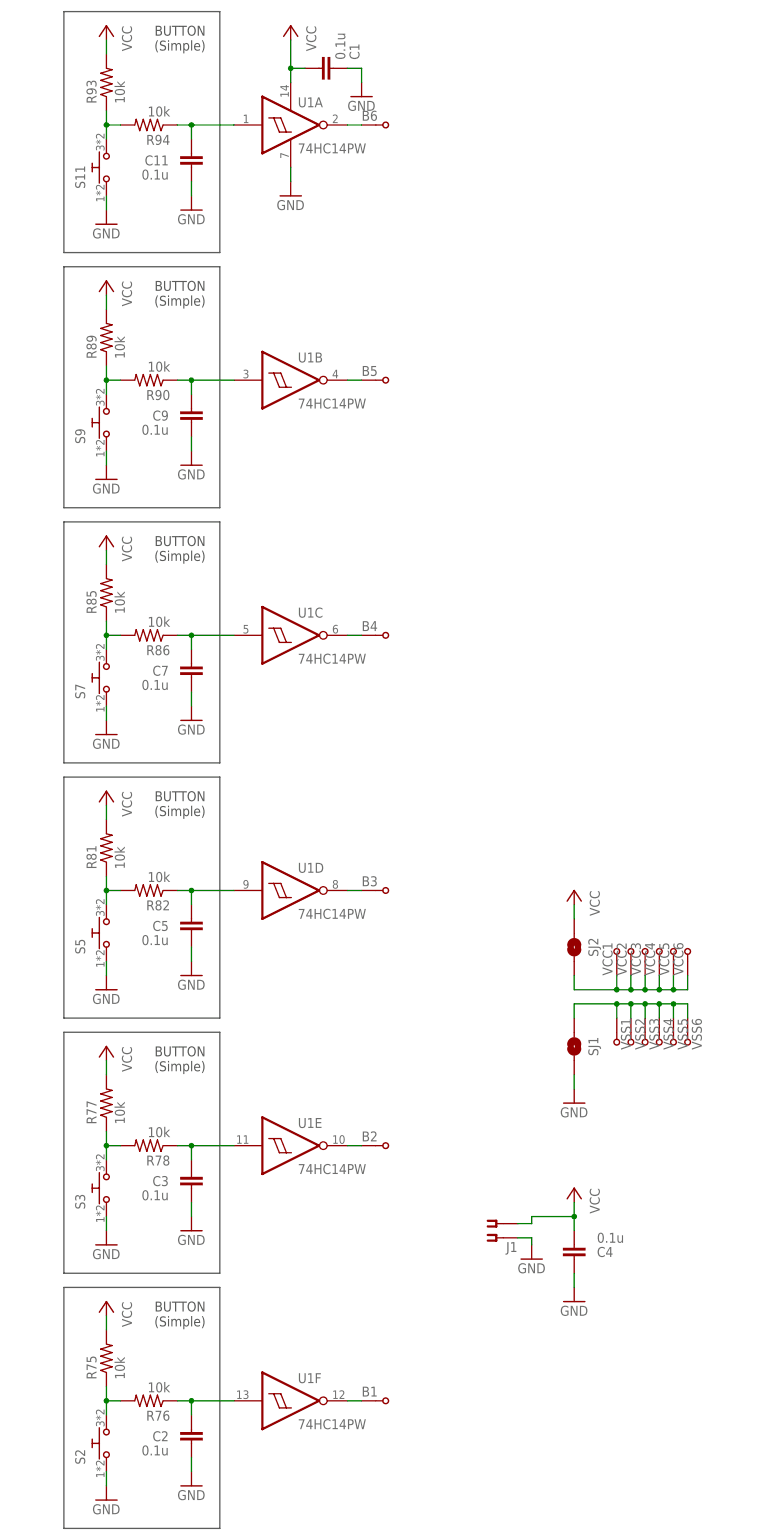
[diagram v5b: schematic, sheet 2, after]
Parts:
- added C1, C4: 0.1u, ellajameson-core:CAP0603
- added J1: (no value), ellajameson-core:CON-F-2SCREWTERM-0.1"
- added SJ1, SJ2: SJ_NO, ellajameson-core:SJ_NO
- added VCC1, VCC2, VCC3, VCC4, VCC5, VCC6, VSS1, VSS2, VSS3, VSS4, VSS5, VSS6: TPWIRE, ellajameson-core:TPWIRE
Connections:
- new net N$303: SJ2.2, VCC1.S, VCC2.S, VCC3.S, VCC4.S, VCC5.S, VCC6.S
- new net N$304: SJ1.1, VSS1.S, VSS2.S, VSS3.S, VSS4.S, VSS5.S, VSS6.S
- net GND: now also C1.2, C4.1, J1.S, SJ1.2
- net VCC: now also C1.1, C4.2, J1.S1, SJ2.1
